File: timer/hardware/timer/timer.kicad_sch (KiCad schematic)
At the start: 22 parts, among them J1 Conn_02x05_Odd_Even, U1 74HC590, U2 74HC590, U3 74HC590, U4 74HC590, U5 74HC590, U6 74HC590, U7 74HC688, U8 74HC688, U9 ATF22V10C

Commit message: layout improvements
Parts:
- added R1: 22Ω, Resistor_THT:R_Axial_DIN0207_L6.3mm_D2.5mm_P10.16mm_Horizontal, symbol Device:R
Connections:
- net CLK: no longer U1.11 (CPC), U2.11 (CPC), U3.11 (CPC), U4.11 (CPC), U5.11 (CPC), U6.11 (CPC)
- net at U9.23 (I/O9): now also R1.1
- new net ICLK: R1.2, U1.11 (CPC), U2.11 (CPC), U3.11 (CPC), U4.11 (CPC), U5.11 (CPC), U6.11 (CPC)
- no-connect marks 6 -> 5
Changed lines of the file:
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@@
 	)
 	(no_connect
-		(at 265.43 147.32)
-	)
-	(no_connect
 		(at 240.03 172.72)
 	)
@@
 		)
 	)
-	(global_label "CLK"
+	(global_label "ICLK"
 		(shape input)
 		(at 250.19 63.5 90)
@@
 		)
 		(property "Intersheetrefs" "${INTERSHEET_REFS}"
-			(at 250.19 56.9467 90)
+			(at 250.19 56.3419 90)
 			(effects
 				(font
@@
 		)
 	)
-	(global_label "CLK"
+	(global_label "~{RO}"
 		(shape input)
-		(at 156.21 63.5 90)
+		(at 238.76 162.56 180)
 		(fields_autoplaced yes)
 		(effects
@@
 				(size 1.27 1.27)
 			)
-			(justify left)
+			(justify right)
 		)
 		(property "Intersheetrefs" "${INTERSHEET_REFS}"
-			(at 156.21 56.9467 90)
+			(at 233.1743 162.56 0)
 			(effects
 				(font
 					(size 1.27 1.27)
 				)
-				(justify left)
+				(justify right)
 				(hide yes)
 			)
 		)
 	)
-	(global_label "~{RO}"
+	(global_label "~{OE3}"
 		(shape input)
-		(at 238.76 162.56 180)
+		(at 304.8 160.02 0)
 		(fields_autoplaced yes)
 		(effects
@@
 				(size 1.27 1.27)
 			)
-			(justify right)
+			(justify left)
 		)
 		(property "Intersheetrefs" "${INTERSHEET_REFS}"
-			(at 233.1743 162.56 0)
+			(at 311.4742 160.02 0)
 			(effects
 				(font
 					(size 1.27 1.27)
 				)
-				(justify right)
+				(justify left)
 				(hide yes)
 			)
 		)
 	)
-	(global_label "~{OE3}"
+	(global_label "LATCH"
 		(shape input)
-		(at 304.8 160.02 0)
+		(at 294.64 63.5 90)
 		(fields_autoplaced yes)
 		(effects
@@
 		)
 		(property "Intersheetrefs" "${INTERSHEET_REFS}"
-			(at 311.4742 160.02 0)
+			(at 294.64 54.83 90)
 			(effects
 				(font
@@
 		)
 	)
-	(global_label "LATCH"
+	(global_label "~{OE5}"
 		(shape input)
-		(at 294.64 63.5 90)
+		(at 304.8 165.1 0)
 		(fields_autoplaced yes)
 		(effects
@@
 		)
 		(property "Intersheetrefs" "${INTERSHEET_REFS}"
-			(at 294.64 54.83 90)
+			(at 311.4742 165.1 0)
 			(effects
 				(font
@@
 		)
 	)
-	(global_label "~{OE5}"
+	(global_label "ICLK"
 		(shape input)
-		(at 304.8 165.1 0)
+		(at 273.05 147.32 0)
 		(fields_autoplaced yes)
 		(effects
@@
 		)
 		(property "Intersheetrefs" "${INTERSHEET_REFS}"
-			(at 311.4742 165.1 0)
+			(at 280.2081 147.32 0)
 			(effects
 				(font
@@
 		)
 	)
-	(global_label "CLK"
+	(global_label "ICLK"
 		(shape input)
 		(at 203.2 63.5 90)
@@
 		)
 		(property "Intersheetrefs" "${INTERSHEET_REFS}"
-			(at 203.2 56.9467 90)
+			(at 203.2 56.3419 90)
 			(effects
 				(font
@@
 		)
 	)
-	(global_label "CLK"
+	(global_label "ICLK"
+		(shape input)
+		(at 156.21 63.5 90)
+		(fields_autoplaced yes)
+		(effects
+			(font
+				(size 1.27 1.27)
+			)
+			(justify left)
+		)
+		(property "Intersheetrefs" "${INTERSHEET_REFS}"
+			(at 156.21 56.3419 90)
+			(effects
+				(font
+					(size 1.27 1.27)
+				)
+				(justify left)
+				(hide yes)
+			)
+		)
+	)
+	(global_label "ICLK"
 		(shape input)
 		(at 344.17 63.5 90)
@@
 		)
 		(property "Intersheetrefs" "${INTERSHEET_REFS}"
-			(at 344.17 56.9467 90)
+			(at 344.17 56.3419 90)
 			(effects
 				(font
@@
 		)
 	)
-	(global_label "CLK"
+	(global_label "ICLK"
 		(shape input)
 		(at 109.22 63.5 90)
@@
 		)
 		(property "Intersheetrefs" "${INTERSHEET_REFS}"
-			(at 109.22 56.9467 90)
+			(at 109.22 56.3419 90)
 			(effects
 				(font
@@
 		)
 	)
-	(global_label "CLK"
+	(global_label "ICLK"
 		(shape input)
 		(at 297.18 63.5 90)
@@
 		)
 		(property "Intersheetrefs" "${INTERSHEET_REFS}"
-			(at 297.18 56.9467 90)
+			(at 297.18 56.3419 90)
 			(effects
 				(font
@@
 					(unit 1)
 				)
+			)
+		)
+	)
+	(symbol
+		(lib_id "Device:R")
+		(at 269.24 147.32 90)
+		(unit 1)
+		(exclude_from_sim no)
+		(in_bom yes)
+		(on_board yes)
+		(dnp no)
+		(property "Reference" "R1"
+			(at 269.24 145.288 90)
+			(effects
+				(font
+					(size 1.27 1.27)
+				)
+			)
+		)
+		(property "Value" "22Ω"
+			(at 269.24 147.32 90)
+			(effects
+				(font
+					(size 1.27 1.27)
+				)
+			)
+		)
+		(property "Footprint" "Resistor_THT:R_Axial_DIN0207_L6.3mm_D2.5mm_P10.16mm_Horizontal"
+			(at 269.24 149.098 90)
+			(effects
+				(font
+					(size 1.27 1.27)
+				)
+				(hide yes)
+			)
+		)
+		(property "Datasheet" "~"
+			(at 269.24 147.32 0)
+			(effects
+				(font
+					(size 1.27 1.27)
+				)
+				(hide yes)
+			)
+		)
+		(property "Description" "Resistor"
+			(at 269.24 147.32 0)
+			(effects
+				(font
+					(size 1.27 1.27)
+				)
+				(hide yes)
+			)
+		)
+		(pin "2"
+		)
+		(pin "1"
+		)
+		(instances
+			(project ""
+				(path "/13a8e646-91ee-46a0-a7f9-7ff532e96a25"
+					(reference "R1")
+					(unit 1)
+				)

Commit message: corrected design flaw in hardware
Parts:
- removed R1: 22Ω, Resistor_THT:R_Axial_DIN0207_L6.3mm_D2.5mm_P10.16mm_Horizontal, symbol Device:R
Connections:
- net GND: now also U1.12 (~{CE}), U2.12 (~{CE}), U3.12 (~{CE}), U4.12 (~{CE}), U5.12 (~{CE})
- net ICLK: now also U9.23 (I/O9); no longer U1.11 (CPC), U2.11 (CPC), U3.11 (CPC), U4.11 (CPC), U5.11 (CPC)
- net at U6.9 (~{RCO}): now also U5.11 (CPC); no longer U5.12 (~{CE})
- net at U5.9 (~{RCO}): now also U4.11 (CPC); no longer U4.12 (~{CE})
- net at U4.9 (~{RCO}): now also U3.11 (CPC); no longer U3.12 (~{CE})
- net at U2.9 (~{RCO}): now also U1.11 (CPC); no longer U1.12 (~{CE})
- net at U3.9 (~{RCO}): now also U2.11 (CPC); no longer U2.12 (~{CE})

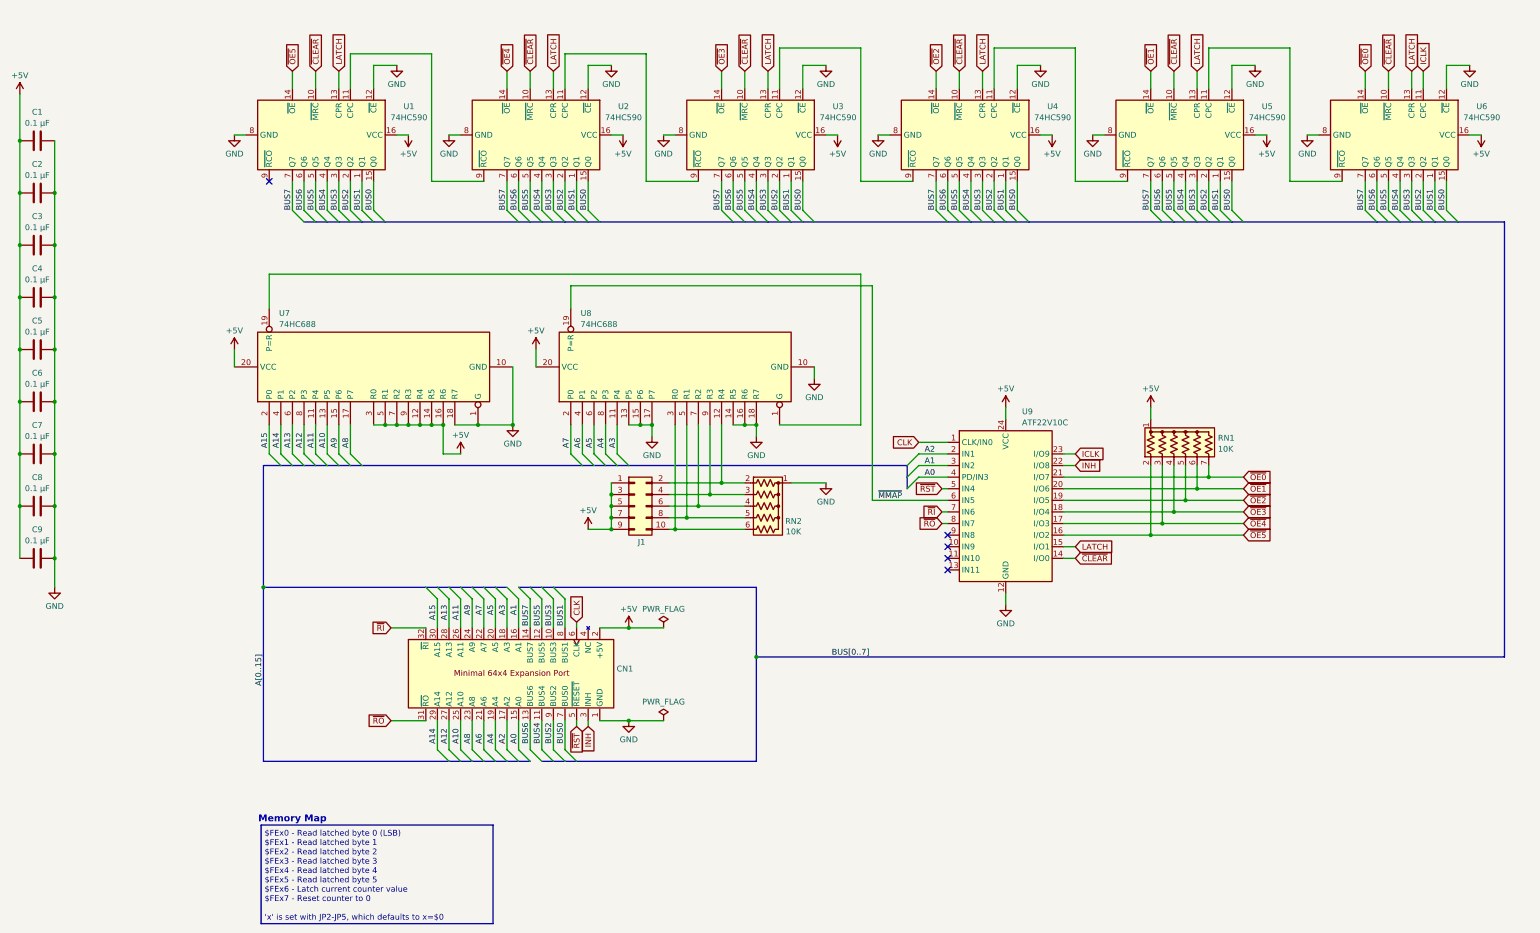
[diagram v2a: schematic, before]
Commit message: improved timer card design
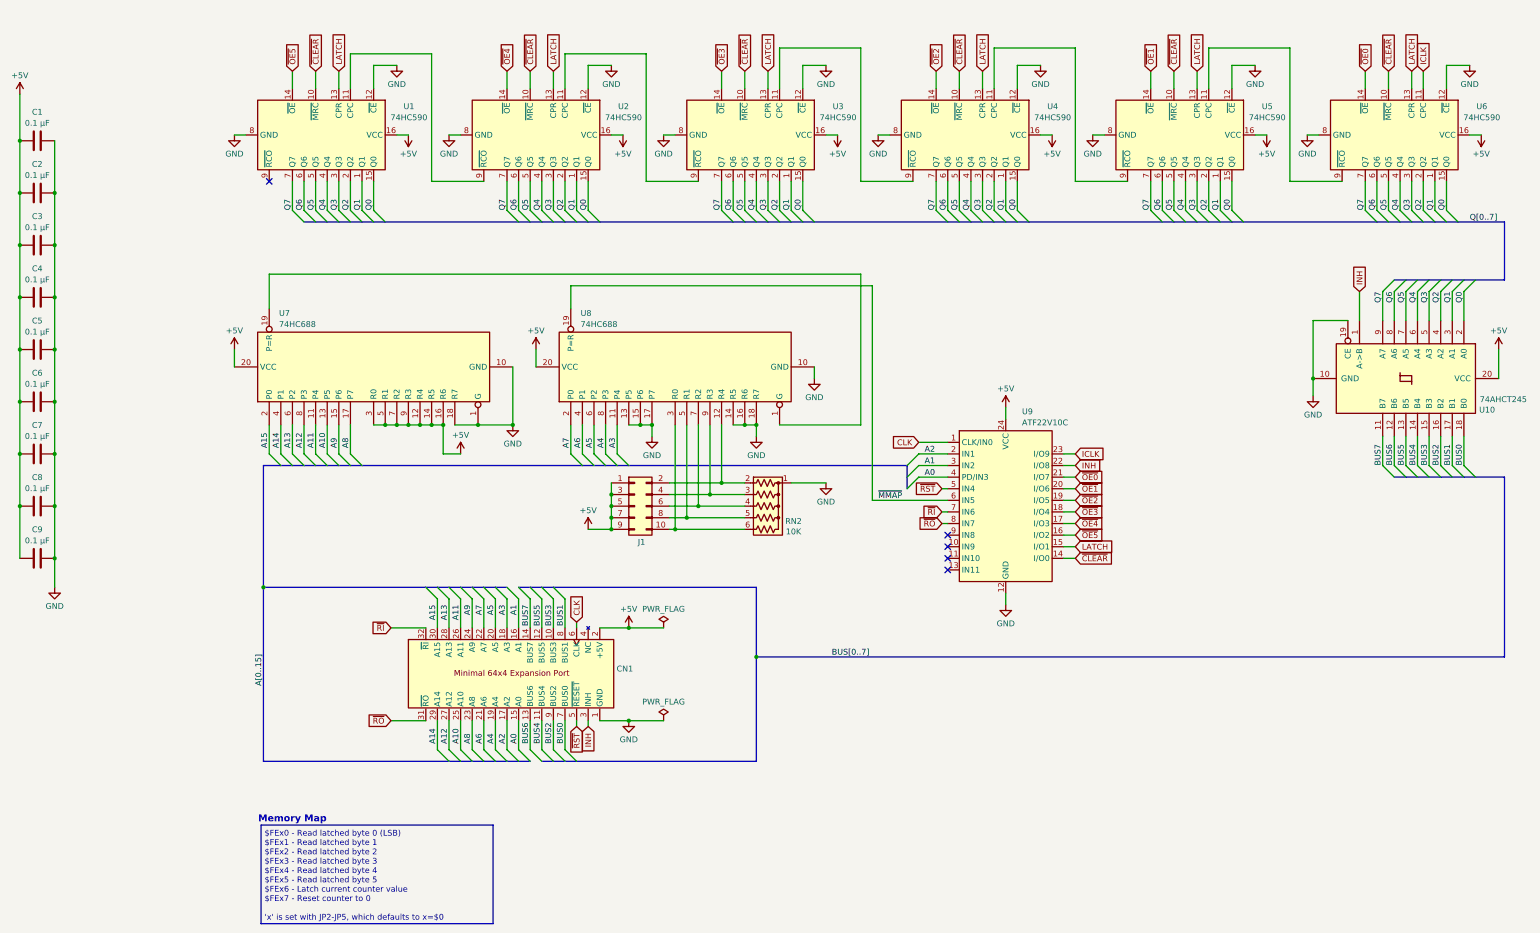
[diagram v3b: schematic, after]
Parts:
- removed RN1: 10K, Resistor_THT:R_Array_SIP7, symbol Device:R_Network06_US
- added U10: 74AHCT245, Package_DIP:DIP-20_W7.62mm_Socket, symbol 74xx:74HC245
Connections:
- net +5V: now also U10.20 (VCC)
- net BUS0: now also U10.18 (B0); no longer U1.15 (Q0), U2.15 (Q0), U3.15 (Q0), U4.15 (Q0), U5.15 (Q0), U6.15 (Q0)
- net BUS1: now also U10.17 (B1); no longer U1.1 (Q1), U2.1 (Q1), U3.1 (Q1), U4.1 (Q1), U5.1 (Q1), U6.1 (Q1)
- net BUS2: now also U10.16 (B2); no longer U1.2 (Q2), U2.2 (Q2), U3.2 (Q2), U4.2 (Q2), U5.2 (Q2), U6.2 (Q2)
- net BUS3: now also U10.15 (B3); no longer U1.3 (Q3), U2.3 (Q3), U3.3 (Q3), U4.3 (Q3), U5.3 (Q3), U6.3 (Q3)
- net BUS4: now also U10.14 (B4); no longer U1.4 (Q4), U2.4 (Q4), U3.4 (Q4), U4.4 (Q4), U5.4 (Q4), U6.4 (Q4)
- net BUS5: now also U10.13 (B5); no longer U1.5 (Q5), U2.5 (Q5), U3.5 (Q5), U4.5 (Q5), U5.5 (Q5), U6.5 (Q5)
- net BUS6: now also U10.12 (B6); no longer U1.6 (Q6), U2.6 (Q6), U3.6 (Q6), U4.6 (Q6), U5.6 (Q6), U6.6 (Q6)
- net BUS7: now also U10.11 (B7); no longer U1.7 (Q7), U2.7 (Q7), U3.7 (Q7), U4.7 (Q7), U5.7 (Q7), U6.7 (Q7)
- net GND: now also U10.10 (GND), U10.19 (CE)
- net INH: now also U10.1 (A->B)
- new net Q0: U1.15 (Q0), U10.2 (A0), U2.15 (Q0), U3.15 (Q0), U4.15 (Q0), U5.15 (Q0), U6.15 (Q0)
- new net Q1: U1.1 (Q1), U10.3 (A1), U2.1 (Q1), U3.1 (Q1), U4.1 (Q1), U5.1 (Q1), U6.1 (Q1)
- new net Q2: U1.2 (Q2), U10.4 (A2), U2.2 (Q2), U3.2 (Q2), U4.2 (Q2), U5.2 (Q2), U6.2 (Q2)
- new net Q3: U1.3 (Q3), U10.5 (A3), U2.3 (Q3), U3.3 (Q3), U4.3 (Q3), U5.3 (Q3), U6.3 (Q3)
- new net Q4: U1.4 (Q4), U10.6 (A4), U2.4 (Q4), U3.4 (Q4), U4.4 (Q4), U5.4 (Q4), U6.4 (Q4)
- new net Q5: U1.5 (Q5), U10.7 (A5), U2.5 (Q5), U3.5 (Q5), U4.5 (Q5), U5.5 (Q5), U6.5 (Q5)
- new net Q6: U1.6 (Q6), U10.8 (A6), U2.6 (Q6), U3.6 (Q6), U4.6 (Q6), U5.6 (Q6), U6.6 (Q6)
- new net Q7: U1.7 (Q7), U10.9 (A7), U2.7 (Q7), U3.7 (Q7), U4.7 (Q7), U5.7 (Q7), U6.7 (Q7)
